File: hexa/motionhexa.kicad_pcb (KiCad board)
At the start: 2 copper layers, 62 x 53.7 mm, 170 parts, among them J2 Conn_01x13_Socket

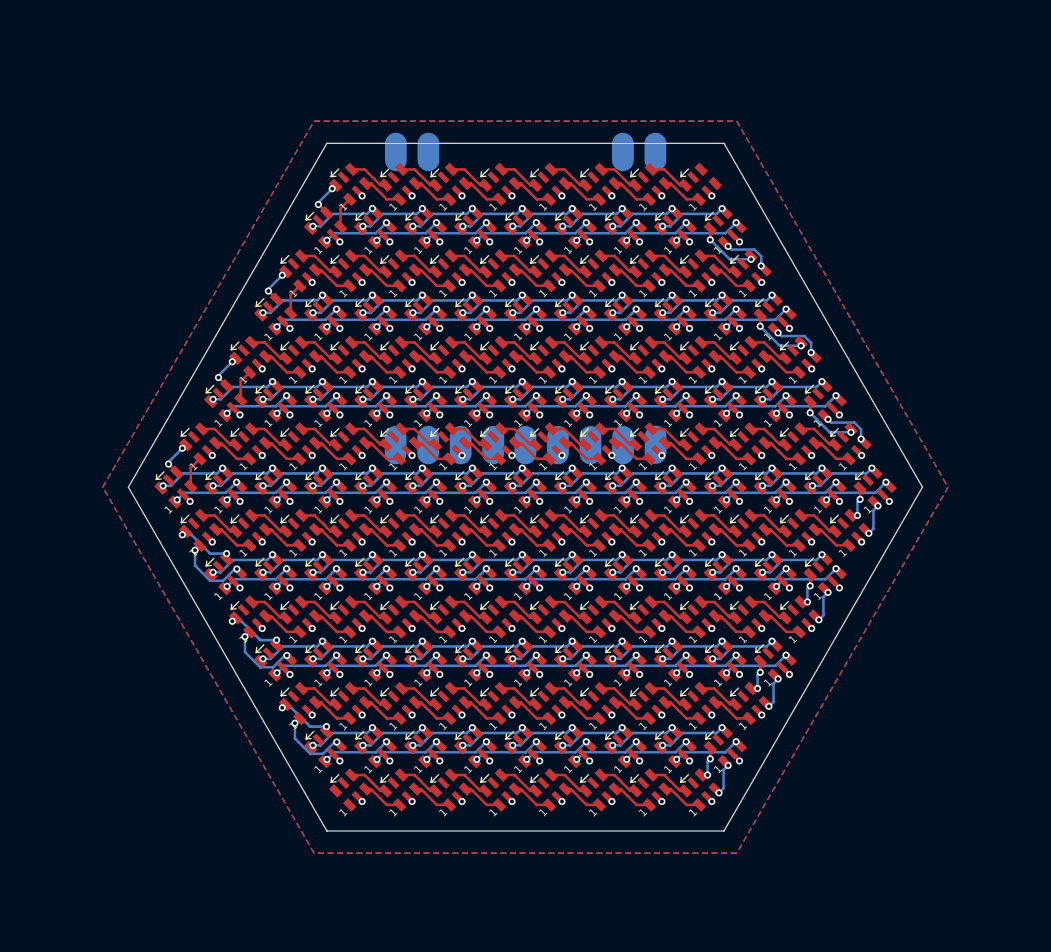
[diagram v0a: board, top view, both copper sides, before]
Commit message: checkpoint - hexa design at a size to host two control boards; add board with an rp2040 and a 9dof imu; add a wip for a second board prototype using a BQ25895M to drive higher currents and charge parallel batteries
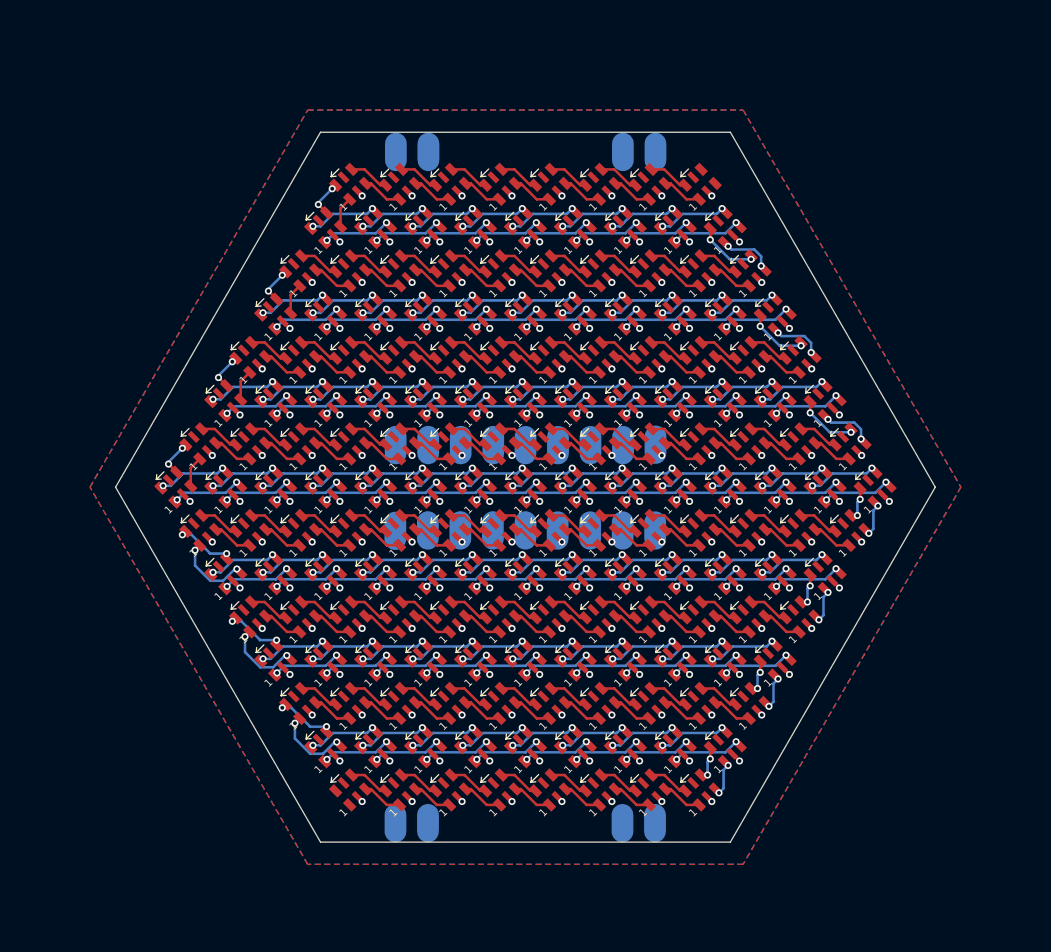
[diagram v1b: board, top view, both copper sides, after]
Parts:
- added J1: Conn_01x13_Socket, motionhexa:lipoparallel_pads, B.Cu at (100.0, 126.2)
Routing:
- net (no net): track 1597.0 -> 1594.5 mm, vias 508 -> 503
- net unconnected-(J1-Pin_9-Pad9): track 0.00 -> 0.50 mm, vias 0 -> 1
- net unconnected-(J1-Pin_8-Pad8): track 0.00 -> 0.50 mm, vias 0 -> 1
- net unconnected-(J1-Pin_5-Pad5): track 0.00 -> 0.50 mm, vias 0 -> 1
- net unconnected-(J1-Pin_6-Pad6): track 0.00 -> 0.50 mm, vias 0 -> 1
- net unconnected-(J1-Pin_11-Pad11): track 0.00 -> 0.50 mm, vias 0 -> 1
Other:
- board size 62 x 53.7 mm -> 64 x 55.4 mm

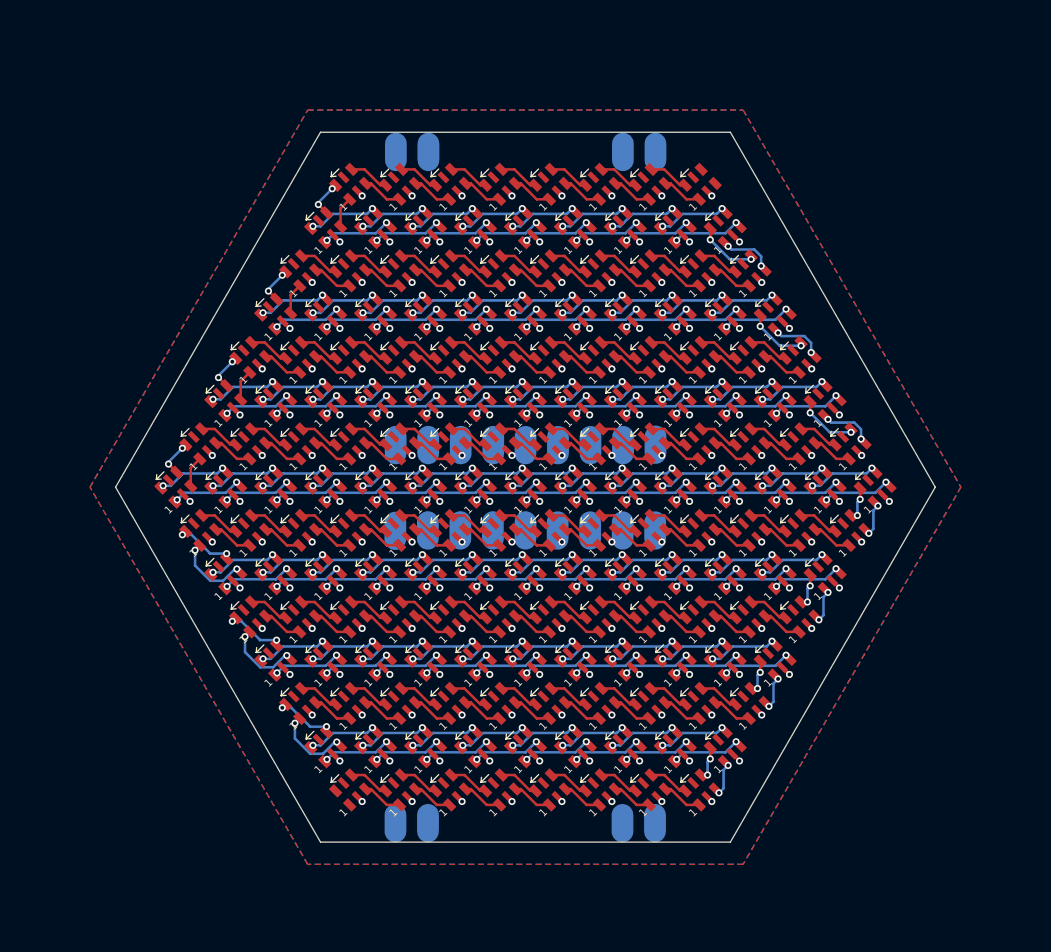
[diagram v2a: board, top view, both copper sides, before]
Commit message: concept of running rpmotion from SYS line on lipo_parallel so we can still control OTG in software
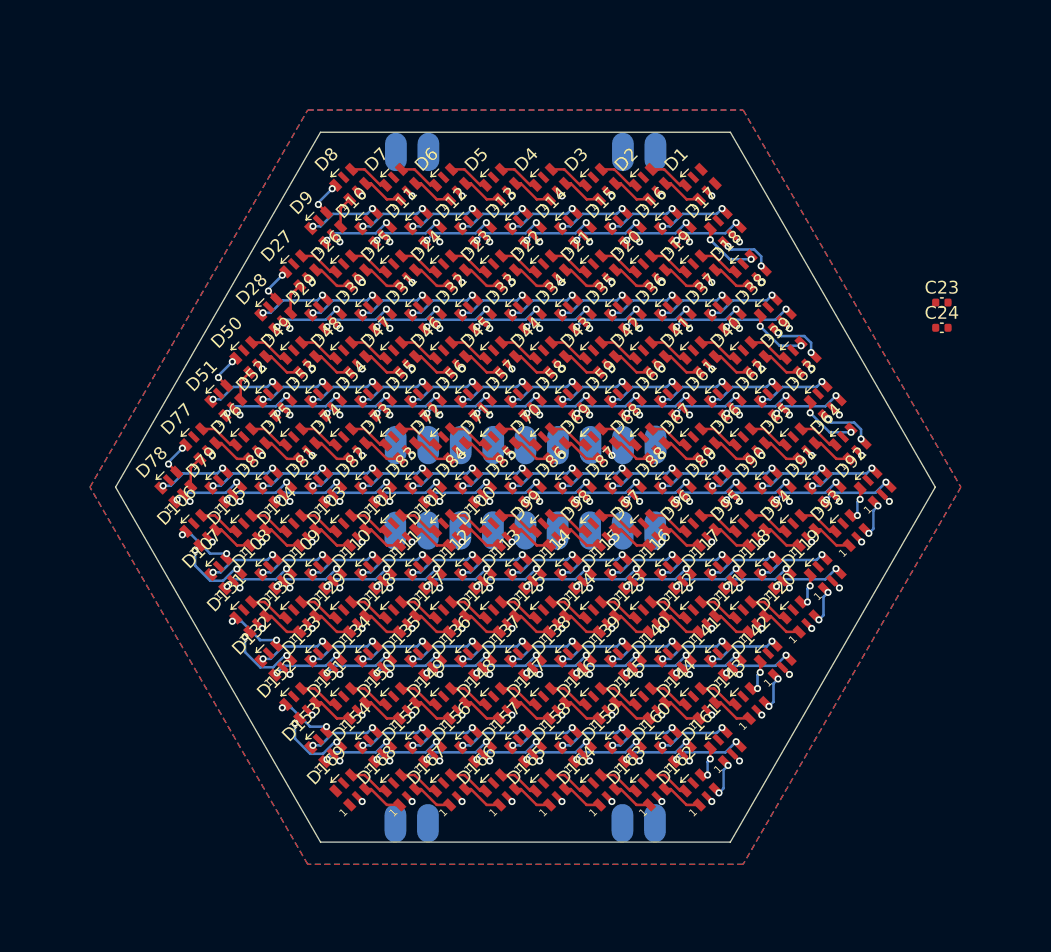
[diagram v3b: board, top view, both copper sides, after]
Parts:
- added C23: 10u, Capacitor_SMD:C_0402_1005Metric, F.Cu at (132.5, 85.6)
- added C24: 10u, Capacitor_SMD:C_0402_1005Metric, F.Cu at (132.5, 87.6)
- D1, D10, D100, D101, D102, D103, D104, D105, D106, D107, D108, D109, D11, D110, D111, D112, D113, D114, D115, D116, D117, D118, D119, D12, D120, D121, D122, D123, D124, D125, D126, D127, D128, D129, D13, D130, D131, D132, D133, D134, D135, D136, D137, D138, D139, D14, D140, D141, D142, D143, D144, D145, D146, D147, D148, D149, D15, D150, D151, D152, D153, D154, D155, D156, D157, D158, D159, D16, D160, D161, D162, D163, D164, D165, D166, D167, D168, D169, D17, D18, D19, D2, D20, D21, D22, D23, D24, D25, D26, D27, D28, D29, D3, D30, D31, D32, D33, D34, D35, D36, D37, D38, D39, D4, D40, D41, D42, D43, D44, D45, D46, D47, D48, D49, D5, D50, D51, D52, D53, D54, D55, D56, D57, D58, D59, D6, D60, D61, D62, D63, D64, D65, D66, D67, D68, D69, D7, D70, D71, D72, D73, D74, D75, D76, D77, D78, D79, D8, D80, D81, D82, D83, D84, D85, D86, D87, D88, D89, D9, D90, D91, D92, D93, D94, D95, D96, D97, D98, D99: value LED-SK9822-EC20 -> SK9822-EC20; footprint LED-SK9822-EC20 -> motionhexa:LED-SK9822-EC20
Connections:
- net SCK renamed SPI_SCK
- net TX renamed SPI_TX
- D1 pad 2: (no net) -> GND
- D1 pad 5: (no net) -> +5V
- D10 pad 2: (no net) -> GND
- D10 pad 3: (no net) -> Net-(D10-SDI)
- D10 pad 4: (no net) -> Net-(D10-CKI)
- D10 pad 5: (no net) -> +5V
- D100 pad 2: (no net) -> GND
- D100 pad 3: (no net) -> Net-(D100-SDI)
- D100 pad 4: (no net) -> Net-(D100-CKI)
- D100 pad 5: (no net) -> +5V
- D101 pad 2: (no net) -> GND
- D101 pad 3: (no net) -> Net-(D100-SDO)
- D101 pad 4: (no net) -> Net-(D100-CKO)
- D101 pad 5: (no net) -> +5V
- D102 pad 2: (no net) -> GND
- D102 pad 3: (no net) -> Net-(D101-SDO)
- D102 pad 4: (no net) -> Net-(D101-CKO)
- D102 pad 5: (no net) -> +5V
- D103 pad 2: (no net) -> GND
- D103 pad 3: (no net) -> Net-(D102-SDO)
- D103 pad 4: (no net) -> Net-(D102-CKO)
- D103 pad 5: (no net) -> +5V
- D104 pad 2: (no net) -> GND
- D104 pad 3: (no net) -> Net-(D103-SDO)
- D104 pad 4: (no net) -> Net-(D103-CKO)
- D104 pad 5: (no net) -> +5V
- D105 pad 2: (no net) -> GND
- D105 pad 3: (no net) -> Net-(D104-SDO)
- D105 pad 4: (no net) -> Net-(D104-CKO)
- D105 pad 5: (no net) -> +5V
- D106 pad 2: (no net) -> GND
- D106 pad 3: (no net) -> Net-(D105-SDO)
- D106 pad 4: (no net) -> Net-(D105-CKO)
- D106 pad 5: (no net) -> +5V
- D107 pad 2: (no net) -> GND
- D107 pad 3: (no net) -> Net-(D106-SDO)
- D107 pad 4: (no net) -> Net-(D106-CKO)
- D107 pad 5: (no net) -> +5V
- D108 pad 2: (no net) -> GND
- D108 pad 3: (no net) -> Net-(D107-SDO)
- D108 pad 4: (no net) -> Net-(D107-CKO)
- D108 pad 5: (no net) -> +5V
- D109 pad 2: (no net) -> GND
- D109 pad 3: (no net) -> Net-(D108-SDO)
- D109 pad 4: (no net) -> Net-(D108-CKO)
- D109 pad 5: (no net) -> +5V
- D11 pad 2: (no net) -> GND
- D11 pad 3: (no net) -> Net-(D10-SDO)
- D11 pad 4: (no net) -> Net-(D10-CKO)
- D11 pad 5: (no net) -> +5V
- D110 pad 2: (no net) -> GND
- D110 pad 3: (no net) -> Net-(D109-SDO)
- D110 pad 4: (no net) -> Net-(D109-CKO)
- D110 pad 5: (no net) -> +5V
- D111 pad 2: (no net) -> GND
- D111 pad 3: (no net) -> Net-(D110-SDO)
- D111 pad 4: (no net) -> Net-(D110-CKO)
- D111 pad 5: (no net) -> +5V
- D112 pad 2: (no net) -> GND
- D112 pad 3: (no net) -> Net-(D111-SDO)
- D112 pad 4: (no net) -> Net-(D111-CKO)
- D112 pad 5: (no net) -> +5V
- D113 pad 2: (no net) -> GND
- D113 pad 3: (no net) -> Net-(D112-SDO)
- D113 pad 4: (no net) -> Net-(D112-CKO)
- D113 pad 5: (no net) -> +5V
- D114 pad 2: (no net) -> GND
- D114 pad 3: (no net) -> Net-(D113-SDO)
- D114 pad 4: (no net) -> Net-(D113-CKO)
- D114 pad 5: (no net) -> +5V
- D115 pad 2: (no net) -> GND
- D115 pad 3: (no net) -> Net-(D114-SDO)
- D115 pad 4: (no net) -> Net-(D114-CKO)
- D115 pad 5: (no net) -> +5V
- D116 pad 2: (no net) -> GND
- D116 pad 3: (no net) -> Net-(D115-SDO)
- D116 pad 4: (no net) -> Net-(D115-CKO)
- D116 pad 5: (no net) -> +5V
- D117 pad 2: (no net) -> GND
- D117 pad 3: (no net) -> Net-(D116-SDO)
- D117 pad 4: (no net) -> Net-(D116-CKO)
- D117 pad 5: (no net) -> +5V
- D118 pad 2: (no net) -> GND
- D118 pad 3: (no net) -> Net-(D117-SDO)
- D118 pad 4: (no net) -> Net-(D117-CKO)
- D118 pad 5: (no net) -> +5V
- D119 pad 2: (no net) -> GND
- D119 pad 3: (no net) -> Net-(D118-SDO)
- D119 pad 4: (no net) -> Net-(D118-CKO)
- D119 pad 5: (no net) -> +5V
- D12 pad 2: (no net) -> GND
- D12 pad 3: (no net) -> Net-(D11-SDO)
- D12 pad 4: (no net) -> Net-(D11-CKO)
- D12 pad 5: (no net) -> +5V
- D120 pad 2: (no net) -> GND
- D120 pad 3: (no net) -> Net-(D119-SDO)
- D120 pad 4: (no net) -> Net-(D119-CKO)
- D120 pad 5: (no net) -> +5V
- D121 pad 2: (no net) -> GND
- D121 pad 3: (no net) -> Net-(D120-SDO)
- D121 pad 4: (no net) -> Net-(D120-CKO)
- D121 pad 5: (no net) -> +5V
- D122 pad 2: (no net) -> GND
- D122 pad 3: (no net) -> Net-(D121-SDO)
- D122 pad 4: (no net) -> Net-(D121-CKO)
- D122 pad 5: (no net) -> +5V
- D123 pad 2: (no net) -> GND
- D123 pad 3: (no net) -> Net-(D122-SDO)
- D123 pad 4: (no net) -> Net-(D122-CKO)
- D123 pad 5: (no net) -> +5V
- D124 pad 2: (no net) -> GND
- D124 pad 3: (no net) -> Net-(D123-SDO)
- D124 pad 4: (no net) -> Net-(D123-CKO)
- D124 pad 5: (no net) -> +5V
- D125 pad 2: (no net) -> GND
- D125 pad 3: (no net) -> Net-(D124-SDO)
- D125 pad 4: (no net) -> Net-(D124-CKO)
- D125 pad 5: (no net) -> +5V
- D126 pad 2: (no net) -> GND
- D126 pad 3: (no net) -> Net-(D125-SDO)
- D126 pad 4: (no net) -> Net-(D125-CKO)
- D126 pad 5: (no net) -> +5V
- D127 pad 2: (no net) -> GND
- D127 pad 3: (no net) -> Net-(D126-SDO)
- D127 pad 4: (no net) -> Net-(D126-CKO)
- D127 pad 5: (no net) -> +5V
- D128 pad 2: (no net) -> GND
- D128 pad 3: (no net) -> Net-(D127-SDO)
- D128 pad 4: (no net) -> Net-(D127-CKO)
- D128 pad 5: (no net) -> +5V
- D129 pad 2: (no net) -> GND
- D129 pad 3: (no net) -> Net-(D128-SDO)
- D129 pad 4: (no net) -> Net-(D128-CKO)
- D129 pad 5: (no net) -> +5V
- D13 pad 2: (no net) -> GND
- D13 pad 3: (no net) -> Net-(D12-SDO)
- D13 pad 4: (no net) -> Net-(D12-CKO)
- D13 pad 5: (no net) -> +5V
- D130 pad 2: (no net) -> GND
- D130 pad 3: (no net) -> Net-(D129-SDO)
- D130 pad 4: (no net) -> Net-(D129-CKO)
- D130 pad 5: (no net) -> +5V
- D131 pad 2: (no net) -> GND
- D131 pad 3: (no net) -> Net-(D130-SDO)
- D131 pad 4: (no net) -> Net-(D130-CKO)
- D131 pad 5: (no net) -> +5V
- D132 pad 2: (no net) -> GND
- D132 pad 3: (no net) -> Net-(D131-SDO)
- D132 pad 4: (no net) -> Net-(D131-CKO)
- D132 pad 5: (no net) -> +5V
- D133 pad 2: (no net) -> GND
- D133 pad 3: (no net) -> Net-(D132-SDO)
- D133 pad 4: (no net) -> Net-(D132-CKO)
- D133 pad 5: (no net) -> +5V
- D134 pad 2: (no net) -> GND
- D134 pad 3: (no net) -> Net-(D133-SDO)
- D134 pad 4: (no net) -> Net-(D133-CKO)
- D134 pad 5: (no net) -> +5V
- D135 pad 2: (no net) -> GND
- D135 pad 3: (no net) -> Net-(D134-SDO)
- D135 pad 4: (no net) -> Net-(D134-CKO)
- D135 pad 5: (no net) -> +5V
- D136 pad 2: (no net) -> GND
- D136 pad 3: (no net) -> Net-(D135-SDO)
- D136 pad 4: (no net) -> Net-(D135-CKO)
- D136 pad 5: (no net) -> +5V
- D137 pad 2: (no net) -> GND
- D137 pad 3: (no net) -> Net-(D136-SDO)
- D137 pad 4: (no net) -> Net-(D136-CKO)
- D137 pad 5: (no net) -> +5V
- D138 pad 2: (no net) -> GND
- D138 pad 3: (no net) -> Net-(D137-SDO)
- D138 pad 4: (no net) -> Net-(D137-CKO)
- D138 pad 5: (no net) -> +5V
- D139 pad 2: (no net) -> GND
- D139 pad 3: (no net) -> Net-(D138-SDO)
- D139 pad 4: (no net) -> Net-(D138-CKO)
- D139 pad 5: (no net) -> +5V
- D14 pad 2: (no net) -> GND
- D14 pad 3: (no net) -> Net-(D13-SDO)
- D14 pad 4: (no net) -> Net-(D13-CKO)
- D14 pad 5: (no net) -> +5V
- D140 pad 2: (no net) -> GND
- D140 pad 3: (no net) -> Net-(D139-SDO)
- D140 pad 4: (no net) -> Net-(D139-CKO)
- D140 pad 5: (no net) -> +5V
- D141 pad 2: (no net) -> GND
- D141 pad 3: (no net) -> Net-(D140-SDO)
- D141 pad 4: (no net) -> Net-(D140-CKO)
- D141 pad 5: (no net) -> +5V
- D142 pad 2: (no net) -> GND
- D142 pad 3: (no net) -> Net-(D141-SDO)
- D142 pad 4: (no net) -> Net-(D141-CKO)
- D142 pad 5: (no net) -> +5V
- D143 pad 2: (no net) -> GND
- D143 pad 3: (no net) -> Net-(D142-SDO)
- D143 pad 4: (no net) -> Net-(D142-CKO)
- D143 pad 5: (no net) -> +5V
- D144 pad 2: (no net) -> GND
- D144 pad 3: (no net) -> Net-(D143-SDO)
- D144 pad 4: (no net) -> Net-(D143-CKO)
- D144 pad 5: (no net) -> +5V
- D145 pad 2: (no net) -> GND
- D145 pad 3: (no net) -> Net-(D144-SDO)
- D145 pad 4: (no net) -> Net-(D144-CKO)
- D145 pad 5: (no net) -> +5V
- D146 pad 2: (no net) -> GND
- D146 pad 3: (no net) -> Net-(D145-SDO)
- D146 pad 4: (no net) -> Net-(D145-CKO)
- D146 pad 5: (no net) -> +5V
- D147 pad 2: (no net) -> GND
- D147 pad 3: (no net) -> Net-(D146-SDO)
- D147 pad 4: (no net) -> Net-(D146-CKO)
- D147 pad 5: (no net) -> +5V
- D148 pad 2: (no net) -> GND
- D148 pad 3: (no net) -> Net-(D147-SDO)
- D148 pad 4: (no net) -> Net-(D147-CKO)
- D148 pad 5: (no net) -> +5V
- D149 pad 2: (no net) -> GND
- D149 pad 3: (no net) -> Net-(D148-SDO)
- D149 pad 4: (no net) -> Net-(D148-CKO)
- D149 pad 5: (no net) -> +5V
- D15 pad 2: (no net) -> GND
- D15 pad 3: (no net) -> Net-(D14-SDO)
- D15 pad 4: (no net) -> Net-(D14-CKO)
- D15 pad 5: (no net) -> +5V
- D150 pad 2: (no net) -> GND
- D150 pad 3: (no net) -> Net-(D149-SDO)
- D150 pad 4: (no net) -> Net-(D149-CKO)
- D150 pad 5: (no net) -> +5V
- D151 pad 2: (no net) -> GND
- D151 pad 3: (no net) -> Net-(D150-SDO)
- D151 pad 4: (no net) -> Net-(D150-CKO)
- D151 pad 5: (no net) -> +5V
- D152 pad 2: (no net) -> GND
- D152 pad 3: (no net) -> Net-(D151-SDO)
- D152 pad 4: (no net) -> Net-(D151-CKO)
- D152 pad 5: (no net) -> +5V
- D153 pad 2: (no net) -> GND
- D153 pad 3: (no net) -> Net-(D152-SDO)
- D153 pad 4: (no net) -> Net-(D152-CKO)
- D153 pad 5: (no net) -> +5V
- D154 pad 2: (no net) -> GND
- D154 pad 3: (no net) -> Net-(D153-SDO)
- D154 pad 4: (no net) -> Net-(D153-CKO)
- D154 pad 5: (no net) -> +5V
- D155 pad 2: (no net) -> GND
- D155 pad 3: (no net) -> Net-(D154-SDO)
- D155 pad 4: (no net) -> Net-(D154-CKO)
- D155 pad 5: (no net) -> +5V
- D156 pad 2: (no net) -> GND
- D156 pad 3: (no net) -> Net-(D155-SDO)
- D156 pad 4: (no net) -> Net-(D155-CKO)
- D156 pad 5: (no net) -> +5V
- D157 pad 2: (no net) -> GND
- D157 pad 3: (no net) -> Net-(D156-SDO)
- D157 pad 4: (no net) -> Net-(D156-CKO)
- D157 pad 5: (no net) -> +5V
- D158 pad 2: (no net) -> GND
- D158 pad 3: (no net) -> Net-(D157-SDO)
- D158 pad 4: (no net) -> Net-(D157-CKO)
- D158 pad 5: (no net) -> +5V
- D159 pad 2: (no net) -> GND
- D159 pad 3: (no net) -> Net-(D158-SDO)
- D159 pad 4: (no net) -> Net-(D158-CKO)
- D159 pad 5: (no net) -> +5V
- D16 pad 2: (no net) -> GND
- D16 pad 3: (no net) -> Net-(D15-SDO)
- D16 pad 4: (no net) -> Net-(D15-CKO)
- D16 pad 5: (no net) -> +5V
- D160 pad 2: (no net) -> GND
- D160 pad 3: (no net) -> Net-(D159-SDO)
- D160 pad 4: (no net) -> Net-(D159-CKO)
- D160 pad 5: (no net) -> +5V
- D161 pad 2: (no net) -> GND
- D161 pad 3: (no net) -> Net-(D160-SDO)
- D161 pad 4: (no net) -> Net-(D160-CKO)
- D161 pad 5: (no net) -> +5V
- D162 pad 2: (no net) -> GND
- D162 pad 3: (no net) -> Net-(D161-SDO)
- D162 pad 4: (no net) -> Net-(D161-CKO)
- D162 pad 5: (no net) -> +5V
- D163 pad 2: (no net) -> GND
- D163 pad 3: (no net) -> Net-(D162-SDO)
- D163 pad 4: (no net) -> Net-(D162-CKO)
- D163 pad 5: (no net) -> +5V
- D164 pad 2: (no net) -> GND
- D164 pad 3: (no net) -> Net-(D163-SDO)
- D164 pad 4: (no net) -> Net-(D163-CKO)
- D164 pad 5: (no net) -> +5V
- D165 pad 2: (no net) -> GND
- D165 pad 3: (no net) -> Net-(D164-SDO)
- D165 pad 4: (no net) -> Net-(D164-CKO)
- D165 pad 5: (no net) -> +5V
- D166 pad 2: (no net) -> GND
- D166 pad 3: (no net) -> Net-(D165-SDO)
- D166 pad 4: (no net) -> Net-(D165-CKO)
- D166 pad 5: (no net) -> +5V
- D167 pad 2: (no net) -> GND
- D167 pad 3: (no net) -> Net-(D166-SDO)
- D167 pad 4: (no net) -> Net-(D166-CKO)
- D167 pad 5: (no net) -> +5V
- D168 pad 2: (no net) -> GND
- D168 pad 3: (no net) -> Net-(D167-SDO)
- D168 pad 4: (no net) -> Net-(D167-CKO)
- D168 pad 5: (no net) -> +5V
- D169 pad 2: (no net) -> GND
- D169 pad 3: (no net) -> Net-(D168-SDO)
- D169 pad 4: (no net) -> Net-(D168-CKO)
- D169 pad 5: (no net) -> +5V
- D17 pad 2: (no net) -> GND
- D17 pad 3: (no net) -> Net-(D16-SDO)
- D17 pad 4: (no net) -> Net-(D16-CKO)
- D17 pad 5: (no net) -> +5V
- D18 pad 2: (no net) -> GND
- D18 pad 3: (no net) -> Net-(D17-SDO)
- D18 pad 4: (no net) -> Net-(D17-CKO)
- D18 pad 5: (no net) -> +5V
- D19 pad 2: (no net) -> GND
- D19 pad 3: (no net) -> Net-(D18-SDO)
- D19 pad 4: (no net) -> Net-(D18-CKO)
- D19 pad 5: (no net) -> +5V
- D2 pad 2: (no net) -> GND
- D2 pad 3: (no net) -> Net-(D1-SDO)
- D2 pad 4: (no net) -> Net-(D1-CKO)
- D2 pad 5: (no net) -> +5V
- D20 pad 2: (no net) -> GND
- D20 pad 3: (no net) -> Net-(D19-SDO)
- D20 pad 4: (no net) -> Net-(D19-CKO)
- D20 pad 5: (no net) -> +5V
- D21 pad 2: (no net) -> GND
- D21 pad 3: (no net) -> Net-(D20-SDO)
- D21 pad 4: (no net) -> Net-(D20-CKO)
- D21 pad 5: (no net) -> +5V
- D22 pad 2: (no net) -> GND
- D22 pad 3: (no net) -> Net-(D21-SDO)
- D22 pad 4: (no net) -> Net-(D21-CKO)
- D22 pad 5: (no net) -> +5V
- D23 pad 2: (no net) -> GND
- D23 pad 3: (no net) -> Net-(D22-SDO)
- D23 pad 4: (no net) -> Net-(D22-CKO)
- D23 pad 5: (no net) -> +5V
- D24 pad 2: (no net) -> GND
- D24 pad 3: (no net) -> Net-(D23-SDO)
- D24 pad 4: (no net) -> Net-(D23-CKO)
- D24 pad 5: (no net) -> +5V
- D25 pad 2: (no net) -> GND
- D25 pad 3: (no net) -> Net-(D24-SDO)
- D25 pad 4: (no net) -> Net-(D24-CKO)
- D25 pad 5: (no net) -> +5V
- D26 pad 2: (no net) -> GND
- D26 pad 3: (no net) -> Net-(D25-SDO)
- D26 pad 4: (no net) -> Net-(D25-CKO)
- D26 pad 5: (no net) -> +5V
- D27 pad 2: (no net) -> GND
- D27 pad 3: (no net) -> Net-(D26-SDO)
- D27 pad 4: (no net) -> Net-(D26-CKO)
- D27 pad 5: (no net) -> +5V
- D28 pad 2: (no net) -> GND
- D28 pad 3: (no net) -> Net-(D27-SDO)
- D28 pad 4: (no net) -> Net-(D27-CKO)
- D28 pad 5: (no net) -> +5V
- D29 pad 2: (no net) -> GND
- D29 pad 3: (no net) -> Net-(D28-SDO)
- D29 pad 4: (no net) -> Net-(D28-CKO)
- D29 pad 5: (no net) -> +5V
- D3 pad 2: (no net) -> GND
- D3 pad 3: (no net) -> Net-(D2-SDO)
- D3 pad 4: (no net) -> Net-(D2-CKO)
- D3 pad 5: (no net) -> +5V
- D30 pad 2: (no net) -> GND
- D30 pad 3: (no net) -> Net-(D29-SDO)
- D30 pad 4: (no net) -> Net-(D29-CKO)
- D30 pad 5: (no net) -> +5V
- D31 pad 2: (no net) -> GND
- D31 pad 3: (no net) -> Net-(D30-SDO)
- D31 pad 4: (no net) -> Net-(D30-CKO)
- D31 pad 5: (no net) -> +5V
- D32 pad 2: (no net) -> GND
- D32 pad 3: (no net) -> Net-(D31-SDO)
- D32 pad 4: (no net) -> Net-(D31-CKO)
- D32 pad 5: (no net) -> +5V
- D33 pad 2: (no net) -> GND
- D33 pad 3: (no net) -> Net-(D32-SDO)
- D33 pad 4: (no net) -> Net-(D32-CKO)
- D33 pad 5: (no net) -> +5V
- D34 pad 2: (no net) -> GND
- D34 pad 3: (no net) -> Net-(D33-SDO)
- D34 pad 4: (no net) -> Net-(D33-CKO)
- D34 pad 5: (no net) -> +5V
- D35 pad 2: (no net) -> GND
- D35 pad 3: (no net) -> Net-(D34-SDO)
- D35 pad 4: (no net) -> Net-(D34-CKO)
- D35 pad 5: (no net) -> +5V
- D36 pad 2: (no net) -> GND
- D36 pad 3: (no net) -> Net-(D35-SDO)
- D36 pad 4: (no net) -> Net-(D35-CKO)
- D36 pad 5: (no net) -> +5V
- D37 pad 2: (no net) -> GND
- D37 pad 3: (no net) -> Net-(D36-SDO)
- D37 pad 4: (no net) -> Net-(D36-CKO)
- D37 pad 5: (no net) -> +5V
- D38 pad 2: (no net) -> GND
- D38 pad 3: (no net) -> Net-(D37-SDO)
- D38 pad 4: (no net) -> Net-(D37-CKO)
- D38 pad 5: (no net) -> +5V
- D39 pad 2: (no net) -> GND
- D39 pad 3: (no net) -> Net-(D38-SDO)
- D39 pad 4: (no net) -> Net-(D38-CKO)
- D39 pad 5: (no net) -> +5V
- D4 pad 2: (no net) -> GND
- D4 pad 3: (no net) -> Net-(D3-SDO)
- D4 pad 4: (no net) -> Net-(D3-CKO)
- D4 pad 5: (no net) -> +5V
- D40 pad 2: (no net) -> GND
- D40 pad 3: (no net) -> Net-(D39-SDO)
- D40 pad 4: (no net) -> Net-(D39-CKO)
- D40 pad 5: (no net) -> +5V
- D41 pad 2: (no net) -> GND
- D41 pad 3: (no net) -> Net-(D40-SDO)
- D41 pad 4: (no net) -> Net-(D40-CKO)
- D41 pad 5: (no net) -> +5V
- D42 pad 2: (no net) -> GND
- D42 pad 3: (no net) -> Net-(D41-SDO)
- D42 pad 4: (no net) -> Net-(D41-CKO)
- D42 pad 5: (no net) -> +5V
- D43 pad 2: (no net) -> GND
- D43 pad 3: (no net) -> Net-(D42-SDO)
- D43 pad 4: (no net) -> Net-(D42-CKO)
- D43 pad 5: (no net) -> +5V
- D44 pad 2: (no net) -> GND
- D44 pad 3: (no net) -> Net-(D43-SDO)
- D44 pad 4: (no net) -> Net-(D43-CKO)
- D44 pad 5: (no net) -> +5V
- D45 pad 2: (no net) -> GND
- D45 pad 3: (no net) -> Net-(D44-SDO)
- D45 pad 4: (no net) -> Net-(D44-CKO)
- D45 pad 5: (no net) -> +5V
- D46 pad 2: (no net) -> GND
- D46 pad 3: (no net) -> Net-(D45-SDO)
- D46 pad 4: (no net) -> Net-(D45-CKO)
- D46 pad 5: (no net) -> +5V
- D47 pad 2: (no net) -> GND
- D47 pad 3: (no net) -> Net-(D46-SDO)
- D47 pad 4: (no net) -> Net-(D46-CKO)
- D47 pad 5: (no net) -> +5V
- D48 pad 2: (no net) -> GND
- D48 pad 3: (no net) -> Net-(D47-SDO)
- D48 pad 4: (no net) -> Net-(D47-CKO)
- D48 pad 5: (no net) -> +5V
- D49 pad 2: (no net) -> GND
- D49 pad 3: (no net) -> Net-(D48-SDO)
- D49 pad 4: (no net) -> Net-(D48-CKO)
- D49 pad 5: (no net) -> +5V
- D5 pad 2: (no net) -> GND
- D5 pad 3: (no net) -> Net-(D4-SDO)
- D5 pad 4: (no net) -> Net-(D4-CKO)
- D5 pad 5: (no net) -> +5V
- D50 pad 2: (no net) -> GND
- D50 pad 3: (no net) -> Net-(D49-SDO)
- D50 pad 4: (no net) -> Net-(D49-CKO)
- D50 pad 5: (no net) -> +5V
- D51 pad 2: (no net) -> GND
- D51 pad 3: (no net) -> Net-(D50-SDO)
- D51 pad 4: (no net) -> Net-(D50-CKO)
- D51 pad 5: (no net) -> +5V
- D52 pad 2: (no net) -> GND
- D52 pad 3: (no net) -> Net-(D51-SDO)
- D52 pad 4: (no net) -> Net-(D51-CKO)
- D52 pad 5: (no net) -> +5V
- D53 pad 2: (no net) -> GND
- D53 pad 3: (no net) -> Net-(D52-SDO)
- D53 pad 4: (no net) -> Net-(D52-CKO)
- D53 pad 5: (no net) -> +5V
- D54 pad 2: (no net) -> GND
- D54 pad 3: (no net) -> Net-(D53-SDO)
- D54 pad 4: (no net) -> Net-(D53-CKO)
- D54 pad 5: (no net) -> +5V
- D55 pad 2: (no net) -> GND
- D55 pad 3: (no net) -> Net-(D54-SDO)
- D55 pad 4: (no net) -> Net-(D54-CKO)
- D55 pad 5: (no net) -> +5V
- D56 pad 2: (no net) -> GND
- D56 pad 3: (no net) -> Net-(D55-SDO)
- D56 pad 4: (no net) -> Net-(D55-CKO)
- D56 pad 5: (no net) -> +5V
- D57 pad 2: (no net) -> GND
- D57 pad 3: (no net) -> Net-(D56-SDO)
- D57 pad 4: (no net) -> Net-(D56-CKO)
- D57 pad 5: (no net) -> +5V
- D58 pad 2: (no net) -> GND
- D58 pad 3: (no net) -> Net-(D57-SDO)
- D58 pad 4: (no net) -> Net-(D57-CKO)
- D58 pad 5: (no net) -> +5V
- D59 pad 2: (no net) -> GND
- D59 pad 3: (no net) -> Net-(D58-SDO)
- D59 pad 4: (no net) -> Net-(D58-CKO)
- D59 pad 5: (no net) -> +5V
- D6 pad 2: (no net) -> GND
- D6 pad 3: (no net) -> Net-(D5-SDO)
- D6 pad 4: (no net) -> Net-(D5-CKO)
- D6 pad 5: (no net) -> +5V
- D60 pad 2: (no net) -> GND
- D60 pad 3: (no net) -> Net-(D59-SDO)
- D60 pad 4: (no net) -> Net-(D59-CKO)
- D60 pad 5: (no net) -> +5V
- D61 pad 2: (no net) -> GND
- D61 pad 3: (no net) -> Net-(D60-SDO)
- D61 pad 4: (no net) -> Net-(D60-CKO)
- D61 pad 5: (no net) -> +5V
- D62 pad 2: (no net) -> GND
- D62 pad 3: (no net) -> Net-(D61-SDO)
- D62 pad 4: (no net) -> Net-(D61-CKO)
- D62 pad 5: (no net) -> +5V
- D63 pad 2: (no net) -> GND
- D63 pad 3: (no net) -> Net-(D62-SDO)
- D63 pad 4: (no net) -> Net-(D62-CKO)
- D63 pad 5: (no net) -> +5V
- D64 pad 2: (no net) -> GND
- D64 pad 3: (no net) -> Net-(D63-SDO)
- D64 pad 4: (no net) -> Net-(D63-CKO)
- D64 pad 5: (no net) -> +5V
- D65 pad 2: (no net) -> GND
- D65 pad 3: (no net) -> Net-(D64-SDO)
- D65 pad 4: (no net) -> Net-(D64-CKO)
- D65 pad 5: (no net) -> +5V
- D66 pad 2: (no net) -> GND
- D66 pad 3: (no net) -> Net-(D65-SDO)
- D66 pad 4: (no net) -> Net-(D65-CKO)
- D66 pad 5: (no net) -> +5V
- D67 pad 2: (no net) -> GND
- D67 pad 3: (no net) -> Net-(D66-SDO)
- D67 pad 4: (no net) -> Net-(D66-CKO)
- D67 pad 5: (no net) -> +5V
- D68 pad 2: (no net) -> GND
- D68 pad 3: (no net) -> Net-(D67-SDO)
- D68 pad 4: (no net) -> Net-(D67-CKO)
- D68 pad 5: (no net) -> +5V
- D69 pad 2: (no net) -> GND
- D69 pad 3: (no net) -> Net-(D68-SDO)
- D69 pad 4: (no net) -> Net-(D68-CKO)
- D69 pad 5: (no net) -> +5V
- D7 pad 2: (no net) -> GND
- D7 pad 3: (no net) -> Net-(D6-SDO)
- D7 pad 4: (no net) -> Net-(D6-CKO)
- D7 pad 5: (no net) -> +5V
- D70 pad 2: (no net) -> GND
- D70 pad 3: (no net) -> Net-(D69-SDO)
- D70 pad 4: (no net) -> Net-(D69-CKO)
- D70 pad 5: (no net) -> +5V
- D71 pad 2: (no net) -> GND
- D71 pad 3: (no net) -> Net-(D70-SDO)
- D71 pad 4: (no net) -> Net-(D70-CKO)
- D71 pad 5: (no net) -> +5V
- D72 pad 2: (no net) -> GND
- D72 pad 3: (no net) -> Net-(D71-SDO)
- D72 pad 4: (no net) -> Net-(D71-CKO)
- D72 pad 5: (no net) -> +5V
- D73 pad 2: (no net) -> GND
- D73 pad 3: (no net) -> Net-(D72-SDO)
- D73 pad 4: (no net) -> Net-(D72-CKO)
- D73 pad 5: (no net) -> +5V
- D74 pad 2: (no net) -> GND
- D74 pad 3: (no net) -> Net-(D73-SDO)
- D74 pad 4: (no net) -> Net-(D73-CKO)
- D74 pad 5: (no net) -> +5V
- D75 pad 2: (no net) -> GND
- D75 pad 3: (no net) -> Net-(D74-SDO)
- D75 pad 4: (no net) -> Net-(D74-CKO)
- D75 pad 5: (no net) -> +5V
- D76 pad 2: (no net) -> GND
- D76 pad 3: (no net) -> Net-(D75-SDO)
- D76 pad 4: (no net) -> Net-(D75-CKO)
- D76 pad 5: (no net) -> +5V
- D77 pad 2: (no net) -> GND
- D77 pad 3: (no net) -> Net-(D76-SDO)
- D77 pad 4: (no net) -> Net-(D76-CKO)
- D77 pad 5: (no net) -> +5V
- D78 pad 2: (no net) -> GND
- D78 pad 3: (no net) -> Net-(D77-SDO)
- D78 pad 4: (no net) -> Net-(D77-CKO)
- D78 pad 5: (no net) -> +5V
- D79 pad 2: (no net) -> GND
- D79 pad 3: (no net) -> Net-(D78-SDO)
- D79 pad 4: (no net) -> Net-(D78-CKO)
- D79 pad 5: (no net) -> +5V
- D8 pad 2: (no net) -> GND
- D8 pad 3: (no net) -> Net-(D7-SDO)
- D8 pad 4: (no net) -> Net-(D7-CKO)
- D8 pad 5: (no net) -> +5V
- D80 pad 2: (no net) -> GND
- D80 pad 3: (no net) -> Net-(D79-SDO)
- D80 pad 4: (no net) -> Net-(D79-CKO)
- D80 pad 5: (no net) -> +5V
- D81 pad 2: (no net) -> GND
- D81 pad 3: (no net) -> Net-(D80-SDO)
- D81 pad 4: (no net) -> Net-(D80-CKO)
- D81 pad 5: (no net) -> +5V
- D82 pad 2: (no net) -> GND
- D82 pad 3: (no net) -> Net-(D81-SDO)
- D82 pad 4: (no net) -> Net-(D81-CKO)
- D82 pad 5: (no net) -> +5V
- D83 pad 2: (no net) -> GND
- D83 pad 3: (no net) -> Net-(D82-SDO)
- D83 pad 4: (no net) -> Net-(D82-CKO)
- D83 pad 5: (no net) -> +5V
- D84 pad 2: (no net) -> GND
- D84 pad 3: (no net) -> Net-(D83-SDO)
- D84 pad 4: (no net) -> Net-(D83-CKO)
- D84 pad 5: (no net) -> +5V
- D85 pad 2: (no net) -> GND
- D85 pad 3: (no net) -> Net-(D84-SDO)
- D85 pad 4: (no net) -> Net-(D84-CKO)
- D85 pad 5: (no net) -> +5V
- D86 pad 2: (no net) -> GND
- D86 pad 3: (no net) -> Net-(D85-SDO)
- D86 pad 4: (no net) -> Net-(D85-CKO)
- D86 pad 5: (no net) -> +5V
- D87 pad 2: (no net) -> GND
- D87 pad 3: (no net) -> Net-(D86-SDO)
- D87 pad 4: (no net) -> Net-(D86-CKO)
- D87 pad 5: (no net) -> +5V
- D88 pad 2: (no net) -> GND
- D88 pad 3: (no net) -> Net-(D87-SDO)
- D88 pad 4: (no net) -> Net-(D87-CKO)
- D88 pad 5: (no net) -> +5V
- D89 pad 2: (no net) -> GND
- D89 pad 3: (no net) -> Net-(D88-SDO)
- D89 pad 4: (no net) -> Net-(D88-CKO)
- D89 pad 5: (no net) -> +5V
- D9 pad 2: (no net) -> GND
- D9 pad 3: (no net) -> Net-(D8-SDO)
- D9 pad 4: (no net) -> Net-(D8-CKO)
- D9 pad 5: (no net) -> +5V
- D90 pad 2: (no net) -> GND
- D90 pad 3: (no net) -> Net-(D89-SDO)
- D90 pad 4: (no net) -> Net-(D89-CKO)
- D90 pad 5: (no net) -> +5V
- D91 pad 2: (no net) -> GND
- D91 pad 3: (no net) -> Net-(D90-SDO)
- D91 pad 4: (no net) -> Net-(D90-CKO)
- D91 pad 5: (no net) -> +5V
- D92 pad 2: (no net) -> GND
- D92 pad 3: (no net) -> Net-(D91-SDO)
- D92 pad 4: (no net) -> Net-(D91-CKO)
- D92 pad 5: (no net) -> +5V
- D93 pad 2: (no net) -> GND
- D93 pad 3: (no net) -> Net-(D92-SDO)
- D93 pad 4: (no net) -> Net-(D92-CKO)
- D93 pad 5: (no net) -> +5V
- D94 pad 2: (no net) -> GND
- D94 pad 3: (no net) -> Net-(D93-SDO)
- D94 pad 4: (no net) -> Net-(D93-CKO)
- D94 pad 5: (no net) -> +5V
- D95 pad 2: (no net) -> GND
- D95 pad 3: (no net) -> Net-(D94-SDO)
- D95 pad 4: (no net) -> Net-(D94-CKO)
- D95 pad 5: (no net) -> +5V
- D96 pad 2: (no net) -> GND
- D96 pad 3: (no net) -> Net-(D95-SDO)
- D96 pad 4: (no net) -> Net-(D95-CKO)
- D96 pad 5: (no net) -> +5V
- D97 pad 2: (no net) -> GND
- D97 pad 3: (no net) -> Net-(D96-SDO)
- D97 pad 4: (no net) -> Net-(D96-CKO)
- D97 pad 5: (no net) -> +5V
- D98 pad 2: (no net) -> GND
- D98 pad 3: (no net) -> Net-(D97-SDO)
- D98 pad 4: (no net) -> Net-(D97-CKO)
- D98 pad 5: (no net) -> +5V
- D99 pad 2: (no net) -> GND
- D99 pad 3: (no net) -> Net-(D98-SDO)
- D99 pad 4: (no net) -> Net-(D98-CKO)
- D99 pad 5: (no net) -> +5V
- J1 pad 1: unconnected-(J1-Pin_1-Pad1) -> GND
- J1 pad 10: unconnected-(J1-Pin_10-Pad10) -> HOST_VREF
- J1 pad 11: unconnected-(J1-Pin_11-Pad11) -> SDA
- J1 pad 12: unconnected-(J1-Pin_12-Pad12) -> SCL
- J1 pad 13: unconnected-(J1-Pin_13-Pad13) -> OTG
- J1 pad 2: unconnected-(J1-Pin_2-Pad2) -> GND
- J1 pad 3: unconnected-(J1-Pin_3-Pad3) -> GND
- J1 pad 4: unconnected-(J1-Pin_4-Pad4) -> GND
- J1 pad 5: unconnected-(J1-Pin_5-Pad5) -> +5V
- J1 pad 6: unconnected-(J1-Pin_6-Pad6) -> GND
- J1 pad 7: unconnected-(J1-Pin_7-Pad7) -> SYS
- J1 pad 8: unconnected-(J1-Pin_8-Pad8) -> ADC0 <-> ILIM
- J1 pad 9: unconnected-(J1-Pin_9-Pad9) -> GPIO4 <-> INT
- J2 pad 10: unconnected-(J2-Pin_10-Pad10) -> ADC0 <-> ILIM
- J2 pad 11: unconnected-(J2-Pin_11-Pad11) -> SYS
- J2 pad 12: unconnected-(J2-Pin_12-Pad12) -> ~{USBBOOT}
- J2 pad 13: unconnected-(J2-Pin_13-Pad13) -> GND
- J2 pad 5: unconnected-(J2-Pin_5-Pad5) -> GPIO11 <-> OTG
- J2 pad 6: unconnected-(J2-Pin_6-Pad6) -> SCL
- J2 pad 7: unconnected-(J2-Pin_7-Pad7) -> SDA
- J2 pad 8: unconnected-(J2-Pin_8-Pad8) -> +1V8
- J2 pad 9: unconnected-(J2-Pin_9-Pad9) -> GPIO4 <-> INT
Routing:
- net (no net): track 1594.5 -> 4.00 mm, vias 503 -> 7
- net GND: track 0.00 -> 104.8 mm, vias 0 -> 161
- net Net-(D152-SDO): track 0.00 -> 6.29 mm, vias 0 -> 2
- net Net-(D106-SDO): track 0.00 -> 6.29 mm, vias 0 -> 2
- net Net-(D131-SDO): track 0.00 -> 6.29 mm, vias 0 -> 2
- net Net-(D91-CKO): track 0.00 -> 5.91 mm, vias 0 -> 2
- net Net-(D86-CKO): track 0.00 -> 5.91 mm, vias 0 -> 2
- net Net-(D81-CKO): track 0.00 -> 5.91 mm, vias 0 -> 2
- net Net-(D58-CKO): track 0.00 -> 5.91 mm, vias 0 -> 2
- net Net-(D53-CKO): track 0.00 -> 5.91 mm, vias 0 -> 2
- net Net-(D34-CKO): track 0.00 -> 5.91 mm, vias 0 -> 2
- net Net-(D29-CKO): track 0.00 -> 5.91 mm, vias 0 -> 2
- net Net-(D158-CKO): track 0.00 -> 5.91 mm, vias 0 -> 2
- net Net-(D153-CKO): track 0.00 -> 5.91 mm, vias 0 -> 2
- net Net-(D14-CKO): track 0.00 -> 5.91 mm, vias 0 -> 2
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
